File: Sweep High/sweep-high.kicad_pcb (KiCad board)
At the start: 2 copper layers, 232.3 x 95.2 mm, 57 parts, among them J1 AudioJack4dpb, J2 AudioJack4dpb, SW10 SW_Push, SW11 SW_Push, SW11_r1 SW_Push, SW12 SW_Push, SW12_r1 SW_Push, SW13_r1 SW_Push, SW14 SW_Push, SW15 SW_Push, SW15_r1 SW_Push, SW16 SW_Push, SW16_r1 SW_Push, SW17 SW_Push, SW17_r1 SW_Push, SW18 SW_Push, SW18_r1 SW_Push, SW2 SW_Push, SW2 SW_SPDT, SW20 SW_Push, SW20_r1 SW_Push, SW21 SW_Push, SW21_r1 SW_Push, SW2_r1 SW_Push, SW3 SW_Push, SW3_r1 SW_Push, SW4 SW_Push, SW4_r1 SW_Push, SW5 SW_Push, SW5_r1 SW_Push, SW6 SW_Push, SW6_r1 SW_Push, SW7_r1 SW_Push, SW8 SW_Push, SW8_r1 SW_Push, SW9 SW_Push, SW9_r1 SW_Push, U1 ProMicro-kbd, U2 ProMicro-kbd

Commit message: Refactor repository and fix breakaway tabs
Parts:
- removed the REF** at (154.3, 90.6)
- removed the REF** at (149.0, 90.6)
- removed the REF** at (154.3, 111.1)
- removed the REF** at (149.0, 111.1)
- removed the RSW2 at (174.9, 116.8) (x2)
- added RSW2: SW_Push, kbd:SW_SPST_B3U-1000P, B.Cu at (172.0, 116.8)
- added RSW2: SW_Push, kbd:SW_SPST_B3U-1000P, F.Cu at (172.0, 116.8)
- added mouse-bite-5mm-slot: VAL**, Duckyb-Parts:mouse-bite-5mm-slot-with-space-for-track, F.Cu at (150.2, 111.2)
- added mouse-bite-5mm-slot: VAL**, Duckyb-Parts:mouse-bite-5mm-slot-with-space-for-track, F.Cu at (150.2, 90.7)
- moved SW20_r1 2.92 mm to (169.3, 132.5)
- moved Bat+1 2.80 mm to (155.0, 83.5)
- moved BatGND4 2.80 mm to (166.5, 83.5)
- moved G*** 2.80 mm to (215.8, 118.9)
- moved J1 2.80 mm to (154.3, 118.7)
- moved SW11_r1 2.80 mm to (198.6, 82.4)
- moved SW12_r1 2.80 mm to (179.6, 85.0)
- moved SW15_r1 2.80 mm to (217.6, 96.9)
- moved SW16_r1 2.80 mm to (198.6, 101.5)
- moved SW17_r1 2.80 mm to (179.6, 104.0)
- moved SW18_r1 2.80 mm to (236.6, 103.0)
- moved SW2 2.80 mm to (160.9, 84.5)
- moved SW21_r1 2.80 mm to (189.2, 124.4)
- moved SW3_r1 2.80 mm to (236.6, 65.0)
- moved SW4_r1 2.80 mm to (217.6, 58.9)
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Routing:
- net gnd: track 20.7 -> 5.95 mm
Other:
- board size 232.3 x 95.2 mm -> 229.5 x 95.2 mm

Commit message: Add gerbers
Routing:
- net Switch13_r: track 57.4 -> 58.4 mm
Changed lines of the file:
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@@
     (thickness 1.6)
     (drawings 57)
-    (tracks 662)
+    (tracks 664)
     (zones 0)
     (modules 55)
@@
   (segment (start 232.81384 102.924) (end 232.708841 103.028999) (width 0.25) (layer B.Cu) (net 31))
   (segment (start 232.81384 100.442) (end 232.81384 102.924) (width 0.25) (layer B.Cu) (net 31))
-  (segment (start 171.62725 97.50999) (end 168.12924 101.008) (width 0.25) (layer B.Cu) (net 32))
-  (segment (start 174.1047 97.50999) (end 171.62725 97.50999) (width 0.25) (layer B.Cu) (net 32))
-  (segment (start 211.404839 91.962999) (end 213.78784 94.346) (width 0.25) (layer B.Cu) (net 32))
-  (segment (start 186.899152 91.962999) (end 211.404839 91.962999) (width 0.25) (layer B.Cu) (net 32))
-  (segment (start 181.352161 97.50999) (end 186.899152 91.962999) (width 0.25) (layer B.Cu) (net 32))
-  (segment (start 174.1047 97.50999) (end 181.352161 97.50999) (width 0.25) (layer B.Cu) (net 32))
   (segment (start 213.78784 99.496) (end 212.48784 100.796) (width 0.25) (layer B.Cu) (net 32))
   (segment (start 213.78784 94.346) (end 213.78784 99.496) (width 0.25) (layer B.Cu) (net 32))
+  (segment (start 211.404839 91.962999) (end 213.78784 94.346) (width 0.25) (layer B.Cu) (net 32))
+  (segment (start 210.155942 90.714102) (end 211.404839 91.962999) (width 0.25) (layer B.Cu) (net 32))
+  (segment (start 168.12924 101.008) (end 171.62725 97.50999) (width 0.25) (layer B.Cu) (net 32))
+  (segment (start 181.352161 97.50999) (end 186.899152 91.962999) (width 0.25) (layer B.Cu) (net 32))
+  (segment (start 186.899152 91.962999) (end 186.929001 91.962999) (width 0.25) (layer B.Cu) (net 32))
+  (segment (start 186.929001 91.962999) (end 188.177898 90.714102) (width 0.25) (layer B.Cu) (net 32))
+  (segment (start 171.62725 97.50999) (end 181.352161 97.50999) (width 0.25) (layer B.Cu) (net 32))
+  (segment (start 188.177898 90.714102) (end 210.155942 90.714102) (width 0.25) (layer B.Cu) (net 32))
   (segment (start 189.350839 101.232999) (end 193.48584 105.368) (width 0.25) (layer B.Cu) (net 33))
   (segment (start 180.585878 101.232999) (end 189.350839 101.232999) (width 0.25) (layer B.Cu) (net 33))
@@
   (segment (start 185.447938 123.529007) (end 185.447938 129.312163) (width 0.25) (layer B.Cu) (net 35))
   (segment (start 184.849333 122.930402) (end 185.447938 123.529007) (width 0.25) (layer B.Cu) (net 35))
-  (segment (start 167.367241 114.469999) (end 167.367241 129.668337) (width 0.25) (layer B.Cu) (net 36))
-  (segment (start 167.367241 129.668337) (end 164.801943 132.233635) (width 0.25) (layer B.Cu) (net 36))
-  (segment (start 168.12924 113.708) (end 167.367241 114.469999) (width 0.25) (layer B.Cu) (net 36))
   (segment (start 166.143432 137.711821) (end 166.90111 138.469499) (width 0.25) (layer B.Cu) (net 36))
   (segment (start 166.143432 133.575124) (end 166.143432 137.711821) (width 0.25) (layer B.Cu) (net 36))
   (segment (start 164.801943 132.233635) (end 166.143432 133.575124) (width 0.25) (layer B.Cu) (net 36))
+  (segment (start 167.132 129.786738) (end 164.685103 132.233635) (width 0.25) (layer B.Cu) (net 36))
+  (segment (start 168.12924 113.708) (end 167.132 114.70524) (width 0.25) (layer B.Cu) (net 36))
+  (segment (start 167.132 114.70524) (end 167.132 129.786738) (width 0.25) (layer B.Cu) (net 36))
   (segment (start 172.149922 80.663556) (end 172.149922 104.607318) (width 0.25) (layer F.Cu) (net 37))
   (segment (start 174.660878 78.1526) (end 172.149922 80.663556) (width 0.25) (layer F.Cu) (net 37))

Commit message: Enlarge slots to .5mm
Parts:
- SW10, SW11, SW11_r1, SW12, SW12_r1, SW13_r1, SW14, SW15, SW15_r1, SW16, SW16_r1, SW17, SW17_r1, SW18, SW18_r1, SW2, SW20, SW20_r1, SW21, SW21_r1, SW2_r1, SW3, SW3_r1, SW4, SW4_r1, SW5, SW5_r1, SW6, SW6_r1, SW7_r1, SW8, SW8_r1, SW9, SW9_r1: footprint Kailh:keyswitch_cherrymx_alps_choc12_1u -> * duckyb-collection:keyswitch_cherrymx_alps_choc12_slots_1u
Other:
- net class Default removed

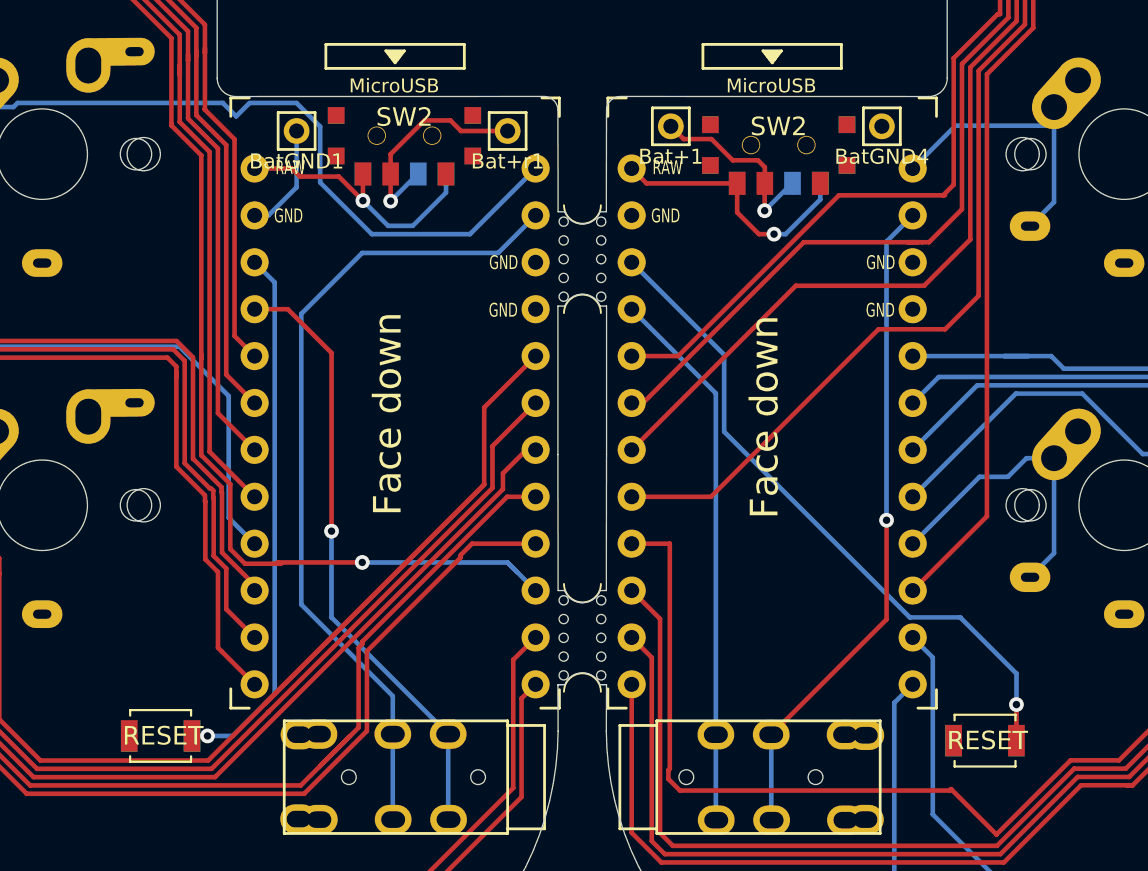
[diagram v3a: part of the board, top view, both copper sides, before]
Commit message: Fix silk screen
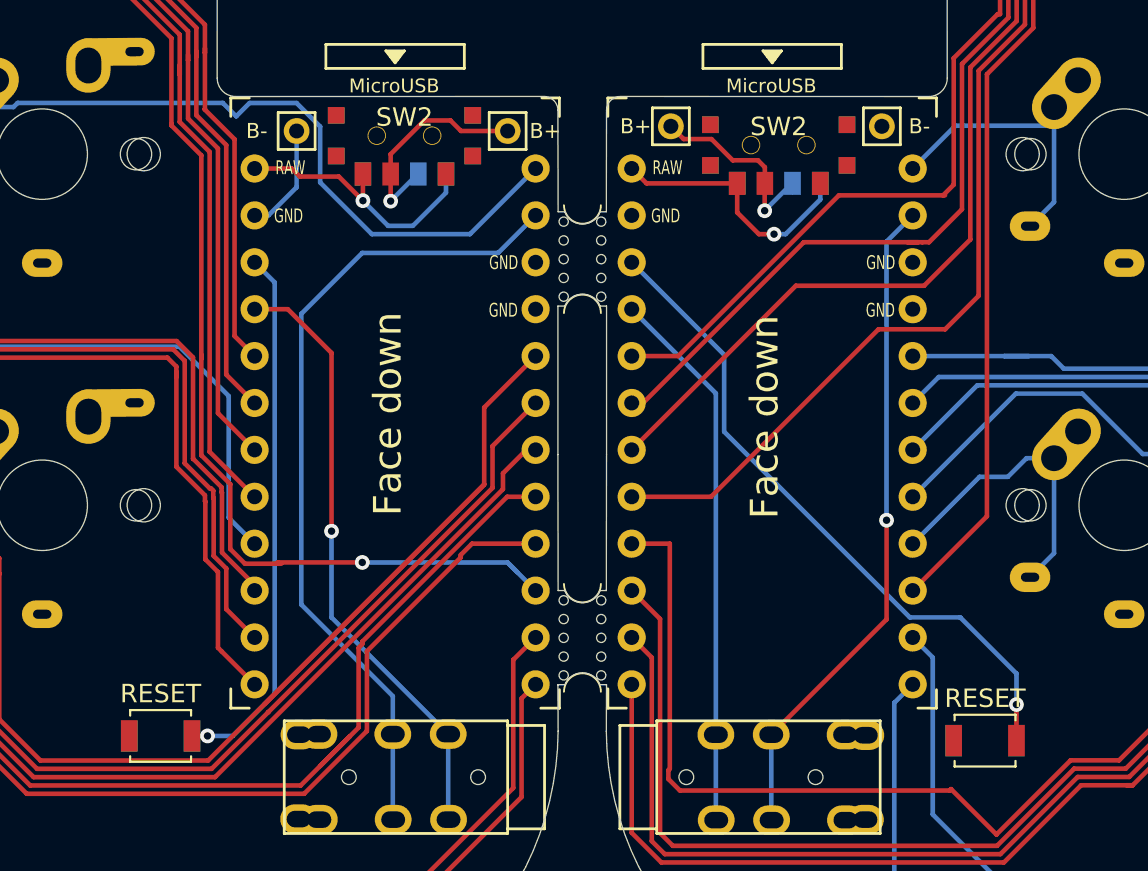
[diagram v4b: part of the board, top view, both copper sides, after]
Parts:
- renumbered Bat+r1 to B+, Bat+1 to B+, BatGND1 to B-, BatGND4 to B-
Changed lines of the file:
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@@
   (net 45 "Net-(SW_POWERR1-Pad1)")
   (footprint "kbd:1pin_conn" (layer "F.Cu")
-    (at 146.19 83.736)
+    (at 146.190005 83.736002)
     (descr "Resitance 3 pas")
     (tags "R")
     (autoplace_cost180 10)
     (attr through_hole)
-    (fp_text reference "Bat+r1" (at 0 1.651) (layer "F.SilkS")
+    (fp_text reference "B+" (at 2.032 0) (layer "F.SilkS")
       (effects (font (size 0.8128 0.8128) (thickness 0.15)))
     )
@@
     (fp_line (start -1 1) (end 1 1) (layer "F.SilkS") (width 0.15))
     (fp_line (start -1 -1) (end -1 1) (layer "F.SilkS") (width 0.15))
-    (pad "1" thru_hole circle locked (at 0 0) (size 1.397 1.397) (drill 0.8128) (layers *.Cu *.Mask "F.SilkS")
+    (pad "1" thru_hole circle (at 0 0) (size 1.397 1.397) (drill 0.8128) (layers *.Cu *.Mask "F.SilkS")
       (net 25 "BT+_r"))
     (model "discret/resistor.wrl"
@@
   )
   (footprint "kbd:1pin_conn" (layer "F.Cu")
-    (at 134.76 83.736)
+    (at 134.760005 83.736002)
     (descr "Resitance 3 pas")
     (tags "R")
     (autoplace_cost180 10)
     (attr through_hole)
-    (fp_text reference "BatGND1" (at 0 1.651) (layer "F.SilkS")
+    (fp_text reference "B-" (at -2.159 0) (layer "F.SilkS")
       (effects (font (size 0.8128 0.8128) (thickness 0.15)))
     )
@@
     (fp_line (start -1 1) (end 1 1) (layer "F.SilkS") (width 0.15))
     (fp_line (start -1 -1) (end -1 1) (layer "F.SilkS") (width 0.15))
-    (pad "1" thru_hole circle locked (at 0 0) (size 1.397 1.397) (drill 0.8128) (layers *.Cu *.Mask "F.SilkS")
+    (pad "1" thru_hole circle (at 0 0) (size 1.397 1.397) (drill 0.8128) (layers *.Cu *.Mask "F.SilkS")
       (net 2 "gnd"))
     (model "discret/resistor.wrl"
@@
       (effects (font (size 1 1) (thickness 0.15)))
     )
-    (fp_text user "RESET" (at 0.127 0) (layer "B.SilkS")
+    (fp_text user "RESET" (at 0 2.286) (layer "B.SilkS")
       (effects (font (size 1 1) (thickness 0.15)) (justify mirror))
     )
@@
     (fp_line (start 1.5 -1.25) (end 1.5 1.25) (layer "F.Fab") (width 0.1))
     (fp_circle (center 0 0) (end 0.75 0) (layer "F.Fab") (width 0.1) (fill none))
-    (pad "1" smd rect locked (at -1.7 0) (size 0.9 1.7) (layers "F.Cu" "F.Paste" "F.Mask")
+    (pad "1" smd rect (at -1.7 0) (size 0.9 1.7) (layers "F.Cu" "F.Paste" "F.Mask")
       (net 2 "gnd"))
-    (pad "2" smd rect locked (at 1.7 0) (size 0.9 1.7) (layers "F.Cu" "F.Paste" "F.Mask")
+    (pad "2" smd rect (at 1.7 0) (size 0.9 1.7) (layers "F.Cu" "F.Paste" "F.Mask")
       (net 5 "reset"))
     (model "${KISYS3DMOD}/Button_Switch_SMD.3dshapes/SW_SPST_B3U-1000P.wrl"
@@
   )
   (footprint "kbd:1pin_conn" (layer "F.Cu")
-    (at 166.45984 83.482)
+    (at 166.45984 83.482002)
     (descr "Resitance 3 pas")
     (tags "R")
     (autoplace_cost180 10)
     (attr through_hole)
-    (fp_text reference "BatGND4" (at 0 1.651) (layer "F.SilkS")
+    (fp_text reference "B-" (at 2.032 0) (layer "F.SilkS")
       (effects (font (size 0.8128 0.8128) (thickness 0.15)))
     )
@@
     (fp_line (start -1 -1) (end -1 1) (layer "F.SilkS") (width 0.15))
     (fp_line (start -1 1) (end 1 1) (layer "F.SilkS") (width 0.15))
-    (pad "1" thru_hole circle locked (at 0 0) (size 1.397 1.397) (drill 0.8128) (layers *.Cu *.Mask "F.SilkS")
+    (pad "1" thru_hole circle (at 0 0) (size 1.397 1.397) (drill 0.8128) (layers *.Cu *.Mask "F.SilkS")
       (net 2 "gnd"))
     (model "discret/resistor.wrl"
@@
       (effects (font (size 1 1) (thickness 0.15)))
     )
-    (fp_text user "RESET" (at 0.127 0) (layer "B.SilkS")
+    (fp_text user "RESET" (at 0 2.286) (layer "B.SilkS")
       (effects (font (size 1 1) (thickness 0.15)) (justify mirror))
     )
@@
     (fp_line (start 1.5 -1.25) (end 1.5 1.25) (layer "F.Fab") (width 0.1))
     (fp_circle (center 0 0) (end 0.75 0) (layer "F.Fab") (width 0.1) (fill none))
-    (pad "1" smd rect locked (at -1.7 0) (size 0.9 1.7) (layers "F.Cu" "F.Paste" "F.Mask")
+    (pad "1" smd rect (at -1.7 0) (size 0.9 1.7) (layers "F.Cu" "F.Paste" "F.Mask")
       (net 2 "gnd"))
-    (pad "2" smd rect locked (at 1.7 0) (size 0.9 1.7) (layers "F.Cu" "F.Paste" "F.Mask")
+    (pad "2" smd rect (at 1.7 0) (size 0.9 1.7) (layers "F.Cu" "F.Paste" "F.Mask")
       (net 27 "reset_r"))
     (model "${KISYS3DMOD}/Button_Switch_SMD.3dshapes/SW_SPST_B3U-1000P.wrl"
@@
   )
   (footprint "kbd:1pin_conn" (layer "F.Cu")
-    (at 155.02984 83.482)
+    (at 155.02984 83.482002)
     (descr "Resitance 3 pas")
     (tags "R")
     (autoplace_cost180 10)
     (attr through_hole)
-    (fp_text reference "Bat+1" (at 0 1.651) (layer "F.SilkS")
+    (fp_text reference "B+" (at -1.905 0) (layer "F.SilkS")
       (effects (font (size 0.8128 0.8128) (thickness 0.15)))
     )
@@
     (fp_line (start -1 -1) (end -1 1) (layer "F.SilkS") (width 0.15))
     (fp_line (start 1 1) (end 1 -1) (layer "F.SilkS") (width 0.15))
-    (pad "1" thru_hole circle locked (at 0 0) (size 1.397 1.397) (drill 0.8128) (layers *.Cu *.Mask "F.SilkS")
+    (pad "1" thru_hole circle (at 0 0) (size 1.397 1.397) (drill 0.8128) (layers *.Cu *.Mask "F.SilkS")
       (net 1 "BT+"))
     (model "discret/resistor.wrl"
@@
     (tags "Tactile Switch")
     (attr smd)
-    (fp_text reference "RSW1" (at 0 -2.55) (layer "B.SilkS") hide
+    (fp_text reference "RSW1" (at 0 -2.55 180) (layer "B.SilkS") hide
       (effects (font (size 1 1) (thickness 0.15)) (justify mirror))
     )
-    (fp_text value "SW_Push" (at 0 2.55) (layer "B.Fab")
+    (fp_text value "SW_Push" (at 0 2.55 180) (layer "B.Fab")
       (effects (font (size 1 1) (thickness 0.15)) (justify mirror))
     )
-    (fp_text user "RESET" (at 0.127 0) (layer "F.SilkS")
+    (fp_text user "RESET" (at 0 -2.286 180) (layer "F.SilkS")
       (effects (font (size 1 1) (thickness 0.15)))
     )
@@
     (fp_line (start 1.5 1.25) (end 1.5 -1.25) (layer "B.Fab") (width 0.1))
     (fp_circle (center 0 0) (end 0.75 0) (layer "B.Fab") (width 0.1) (fill none))
-    (pad "1" smd rect locked (at -1.7 0) (size 0.9 1.7) (layers "B.Cu" "B.Paste" "B.Mask")
+    (pad "1" smd rect (at -1.7 0) (size 0.9 1.7) (layers "B.Cu" "B.Paste" "B.Mask")
       (net 2 "gnd"))
-    (pad "2" smd rect locked (at 1.7 0) (size 0.9 1.7) (layers "B.Cu" "B.Paste" "B.Mask")
+    (pad "2" smd rect (at 1.7 0) (size 0.9 1.7) (layers "B.Cu" "B.Paste" "B.Mask")
       (net 5 "reset"))
     (model "${KISYS3DMOD}/Button_Switch_SMD.3dshapes/SW_SPST_B3U-1000P.wrl"
@@
     (tags "Tactile Switch")
     (attr smd)
-    (fp_text reference "RSW2" (at 0 -2.55) (layer "B.SilkS") hide
+    (fp_text reference "RSW2" (at 0 -2.55 180) (layer "B.SilkS") hide
       (effects (font (size 1 1) (thickness 0.15)) (justify mirror))
     )
-    (fp_text value "SW_Push" (at 0 2.55) (layer "B.Fab")
+    (fp_text value "SW_Push" (at 0 2.55 180) (layer "B.Fab")
       (effects (font (size 1 1) (thickness 0.15)) (justify mirror))
     )
-    (fp_text user "RESET" (at 0.127 0) (layer "F.SilkS")
+    (fp_text user "RESET" (at 0 -2.286 180) (layer "F.SilkS")
       (effects (font (size 1 1) (thickness 0.15)))
     )
@@
     (fp_line (start 1.5 -1.25) (end -1.5 -1.25) (layer "B.Fab") (width 0.1))
     (fp_circle (center 0 0) (end 0.75 0) (layer "B.Fab") (width 0.1) (fill none))
-    (pad "1" smd rect locked (at -1.7 0) (size 0.9 1.7) (layers "B.Cu" "B.Paste" "B.Mask")
+    (pad "1" smd rect (at -1.7 0) (size 0.9 1.7) (layers "B.Cu" "B.Paste" "B.Mask")
       (net 2 "gnd"))
-    (pad "2" smd rect locked (at 1.7 0) (size 0.9 1.7) (layers "B.Cu" "B.Paste" "B.Mask")
+    (pad "2" smd rect (at 1.7 0) (size 0.9 1.7) (layers "B.Cu" "B.Paste" "B.Mask")
       (net 27 "reset_r"))
     (model "${KISYS3DMOD}/Button_Switch_SMD.3dshapes/SW_SPST_B3U-1000P.wrl"

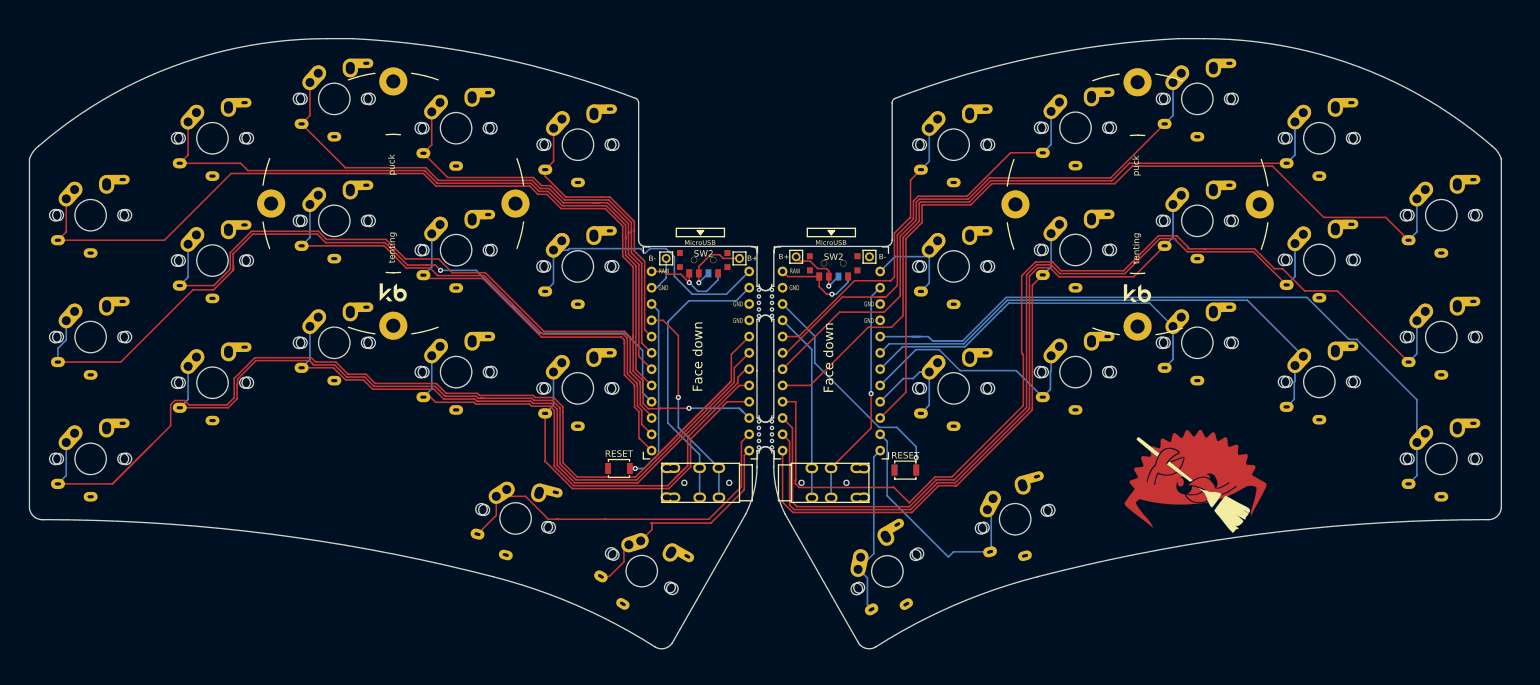
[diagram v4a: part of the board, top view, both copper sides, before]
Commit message: Fix DRC issues on edge
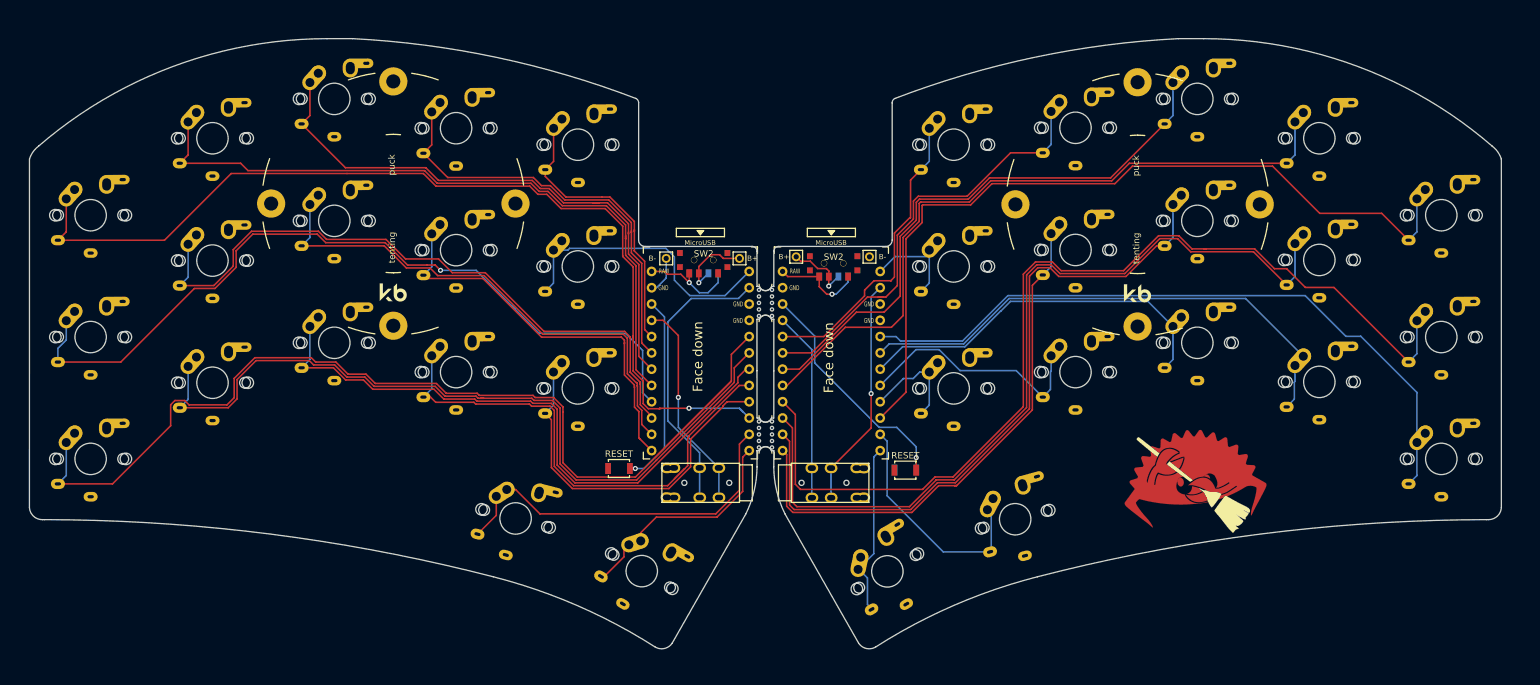
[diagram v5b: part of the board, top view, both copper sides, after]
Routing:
- net Switch11: track 178.4 -> 169.7 mm
- net Switch6_r: track 158.0 -> 154.7 mm
- net Switch16: track 58.2 -> 55.8 mm
- net Switch6: track 125.8 -> 124.9 mm
- net reset: track 30.1 -> 30.9 mm
- net Switch16_r: track 37.3 -> 36.6 mm
- net Switch17: track 34.2 -> 33.7 mm
- net Switch5_r: track 46.9 -> 47.4 mm
